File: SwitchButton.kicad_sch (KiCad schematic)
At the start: 4 parts, among them SW1 SW_Push, SW2 SW_Push

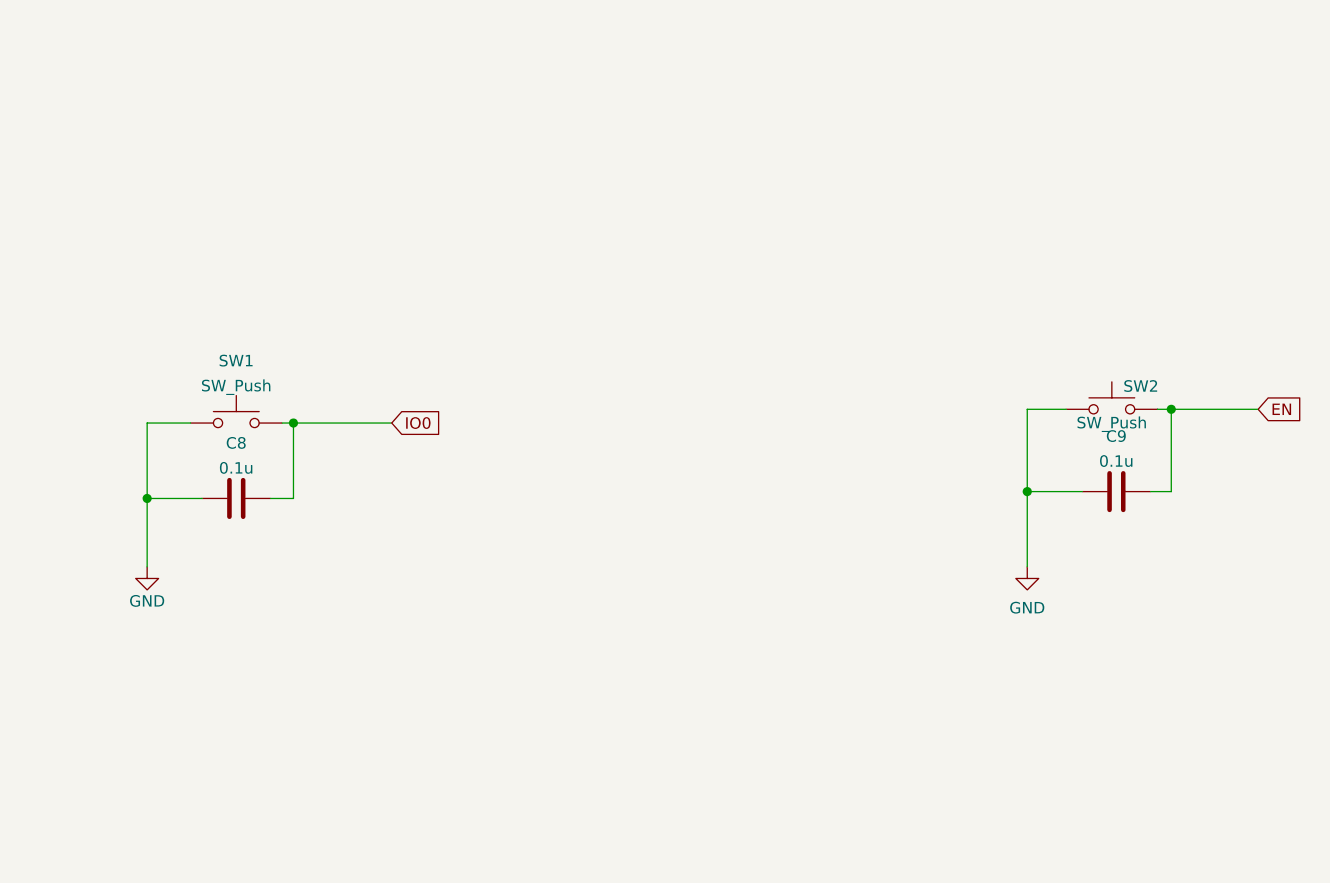
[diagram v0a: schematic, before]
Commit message: Added VOC and Optical Sensors
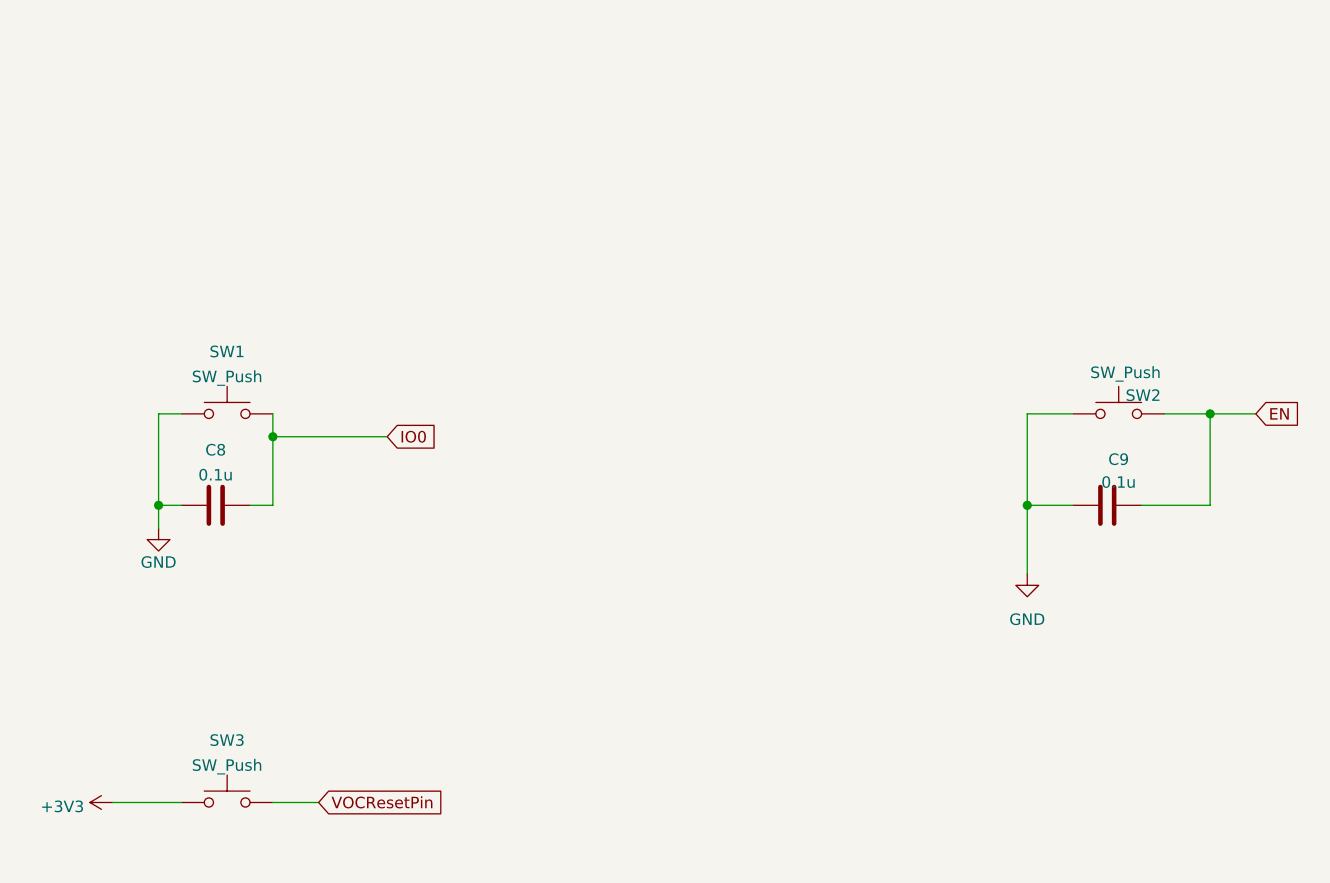
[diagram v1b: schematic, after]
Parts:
- added SW3: SW_Push, Button_Switch_SMD:SW_SPST_TL3342, symbol Switch:SW_Push
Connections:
- new net +3V3: SW3.1
- new net VOCResetPin: SW3.2
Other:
- moved on the sheet: C8, C9, SW1, SW2

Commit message: Vertical Horizontal Traces
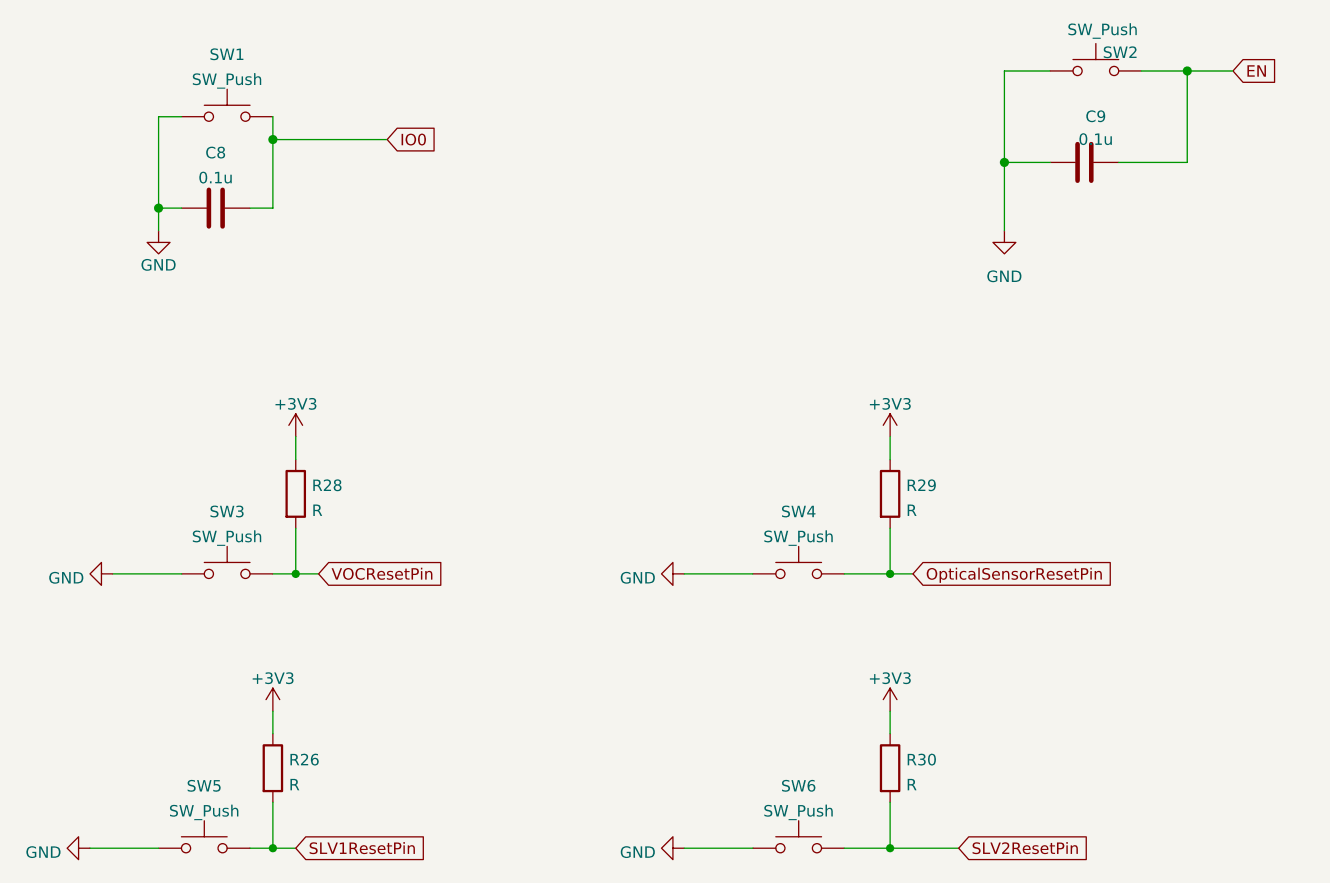
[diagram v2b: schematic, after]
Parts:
- added R26, R28, R29, R30: R, Resistor_SMD:R_0603_1608Metric_Pad0.98x0.95mm_HandSolder, symbol Device:R
- added SW4, SW5, SW6: SW_Push, Button_Switch_SMD:SW_SPST_TL3342, symbol Switch:SW_Push
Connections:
- net +3V3: now also R26.1, R28.1, R29.1, R30.1; no longer SW3.1
- net GND: now also SW3.1, SW4.1, SW5.1, SW6.1
- net VOCResetPin: now also R28.2
- new net OpticalSensorResetPin: R29.2, SW4.2
- new net SLV1ResetPin: R26.2, SW5.2
- new net SLV2ResetPin: R30.2, SW6.2
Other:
- moved on the sheet: C8, C9, SW1, SW2, SW3
